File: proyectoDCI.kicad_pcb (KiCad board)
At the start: 2 copper layers, 45 x 20 mm, 27 parts, among them P1 CONN_02X04, P2 CONN_01X01, P3 GSG-RF-CONN, P4 GSG-RF-CONN, U1 AD5933, U2 ADG849, U3 AD8606, U4 ASFLMB-16.000MHZ-LY-T, U5 ADP150

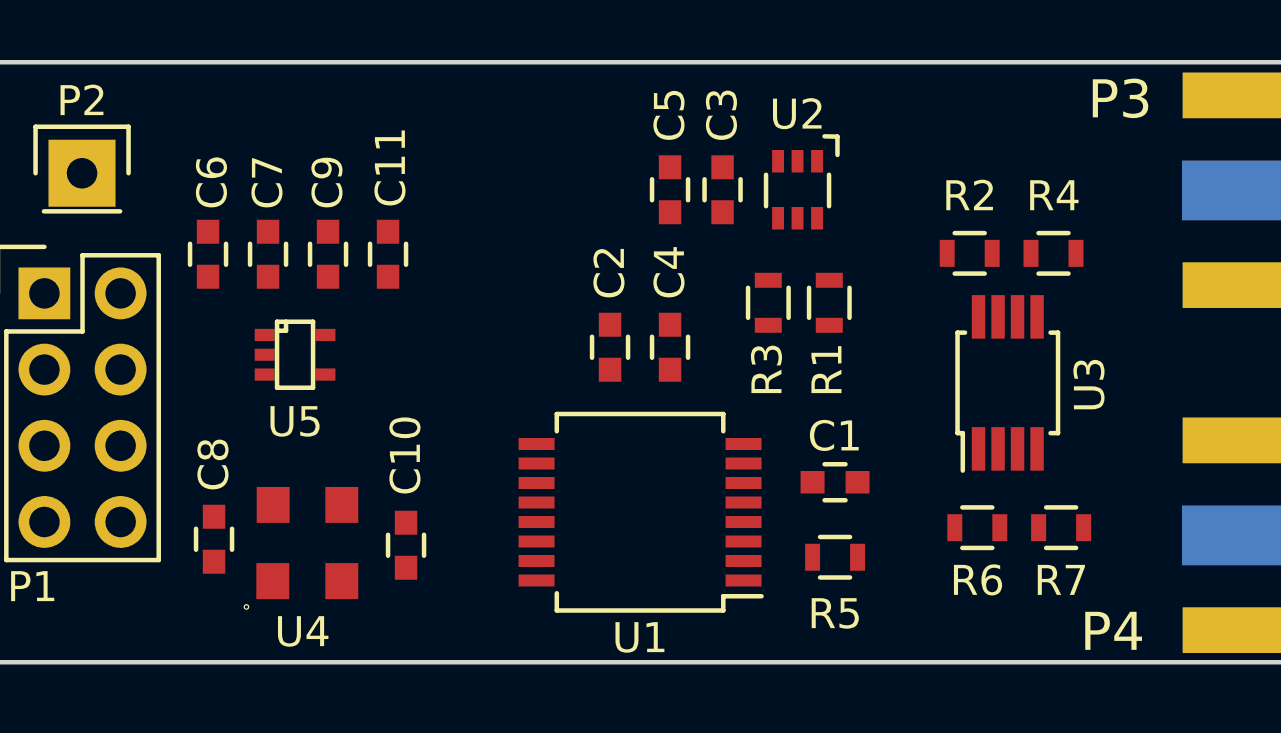
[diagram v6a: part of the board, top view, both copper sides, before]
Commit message: Ruteados los conjuntos por separado
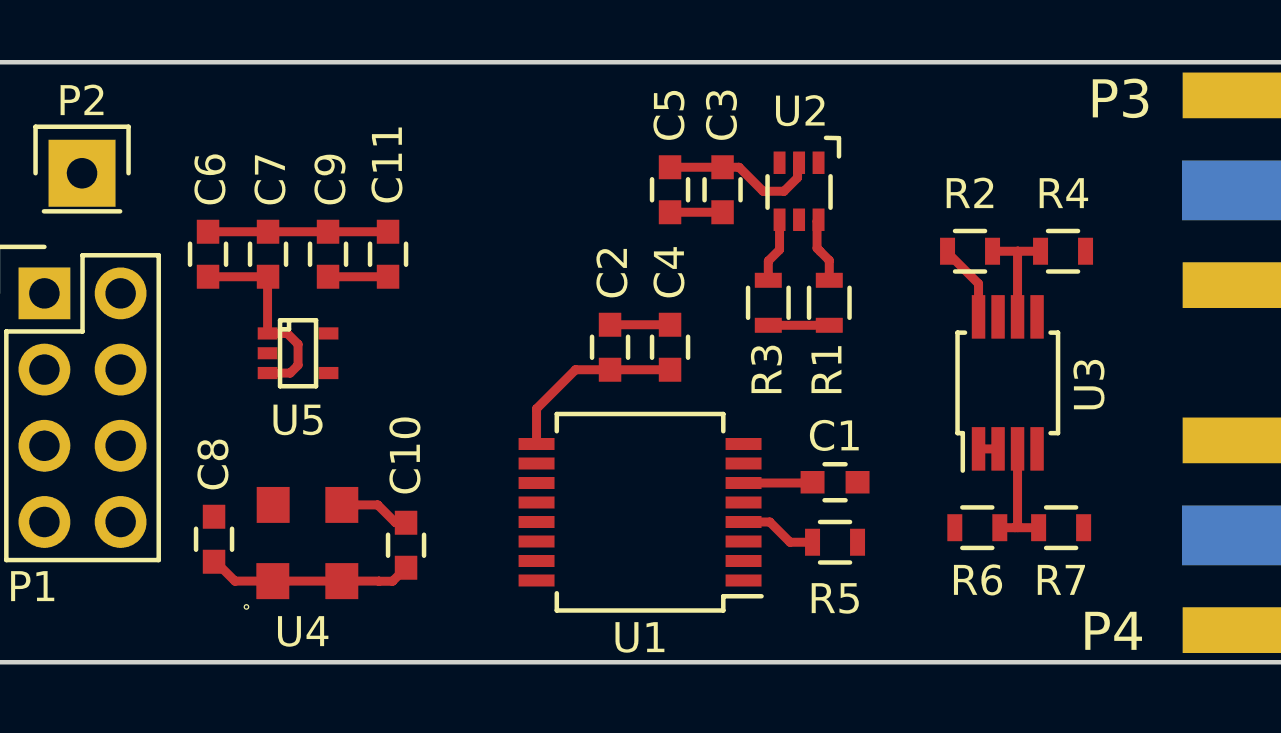
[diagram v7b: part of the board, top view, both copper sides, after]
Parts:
- moved R5 0.50 mm to (178.5, 116.5)
- moved R4 0.33 mm to (186.1, 106.8)
- moved U5 0.11 mm to (160.6, 110.2)
- moved R2 0.07 mm to (183.0, 106.8)
- moved U2 0.07 mm to (177.3, 104.8)
- turned C11 to 90 degrees
- turned C2 to 90 degrees
- turned C4 to 90 degrees
- turned C6 to 90 degrees
- turned C7 to 90 degrees
- turned C9 to 90 degrees
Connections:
- P1 pad 7: /Senal/VCC -> VDD
- P1 pad 8: /Senal/VCC -> VDD
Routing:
- net GND: track 0.00 -> 16.6 mm
- net VDD: track 0.00 -> 13.0 mm
- net VAA: track 0.00 -> 9.93 mm
- net /Senal/VOUT_D: track 0.00 -> 4.02 mm
- net /Senal/VREF: track 0.00 -> 3.80 mm
- net /Senal/RFB: track 0.00 -> 2.58 mm
- net /Otros/MCLK: track 0.00 -> 2.39 mm
- net /Senal/VOUT: track 0.00 -> 2.31 mm
- net /Senal/S2: track 0.00 -> 2.21 mm
- net /Senal/S1: track 0.00 -> 2.17 mm
- net /Senal/CIN: track 0.00 -> 2.03 mm
- net /Senal/COUT: track 0.00 -> 0.65 mm

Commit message: Ruteo completado
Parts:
- P3, P4: moved to B.Cu
- moved P4 2.60 mm to (201.2, 117.6)
- moved P3 2.50 mm to (201.1, 106.0)
- moved R2 0.70 mm to (183.0, 106.1)
- moved R4 0.70 mm to (186.1, 106.1)
- moved U4 0.21 mm to (160.7, 116.5)
- turned C3 to 90 degrees
- turned C5 to 90 degrees
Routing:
- net GND: track 16.6 -> 129.1 mm, vias 0 -> 5
- net VAA: track 9.93 -> 48.2 mm, vias 0 -> 4
- net /Senal/SEL: track 0.00 -> 25.9 mm, vias 0 -> 2
- net /Senal/VIN: track 0.00 -> 25.0 mm, vias 0 -> 3
- net /Senal/SCL: track 0.00 -> 22.8 mm, vias 0 -> 1
- net VDD: track 13.0 -> 35.7 mm
- net /Senal/SDA: track 0.00 -> 20.8 mm, vias 0 -> 1
- net /Senal/CIN: track 2.03 -> 20.6 mm
- net /Otros/MCLK: track 2.39 -> 20.0 mm, vias 0 -> 2
- net /Senal/COUT: track 0.65 -> 12.3 mm
- net /Senal/VOUT_D: track 4.02 -> 12.7 mm
